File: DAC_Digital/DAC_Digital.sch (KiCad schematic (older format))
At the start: 118 parts

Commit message: Update IACSense
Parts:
- added D?: SMCJ5.0A-TR, symbol D_TVS
- added F?: FUSE_CLIP_5x20, symbol FUSE_CLIP_5x20
- added J?: Conn_01x02, symbol Conn_01x02
- U?: footprint Mobi_library:QFN36-0.5 -> Housings_DFN_QFN:QFN-36-1EP_6x6mm_Pitch0.5mm
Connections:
- net labels removed: GND
- wire segments 510 -> 521

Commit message: update footprint
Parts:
- C? (x6): footprint Mobi_library:SM0402-MR -> Yame_library:SM0603-MR
- C? (x7), R? (x5): footprint (none) -> Yame_library:SM0603-MR
- U? (x2): value 74AHC1G08 -> 74LVC1G08
- X?: footprint Mobi_library:7A_SERIES_TXC -> Yame_library:7A_SERIES_TXC
- Y?: footprint (none) -> Crystals:Crystal_HC49-U_Vertical
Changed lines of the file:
@@
 F 0 "X?" H 11150 7200 60  0000 C CNN
 F 1 "7A-24.000MAAJ-T" H 11350 6700 60  0000 C CNN
-F 2 "Mobi_library:7A_SERIES_TXC" H 11300 6950 60  0001 C CNN
+F 2 "Yame_library:7A_SERIES_TXC" H 11300 6950 60  0001 C CNN
 F 3 "~" H 11300 6950 60  0000 C CNN
 F 4 "Crystals 24.000MHz 30ppm -20 +70C 18pF" H 11300 6950 60  0001 C CNN "Supplier Ref."
@@
 F 0 "C?" H 14650 3600 40  0000 L CNN
 F 1 "100n" H 14656 3415 40  0000 L CNN
-F 2 "Mobi_library:SM0402-MR" H 14688 3350 30  0001 C CNN
+F 2 "Yame_library:SM0603-MR" H 14688 3350 30  0001 C CNN
 F 3 "~" H 14650 3500 60  0000 C CNN
 F 4 "Capacitor MLCC 100nF 0402 10V (min.) 10%" H 14650 3500 60  0001 C CNN "Supplier Ref."
@@
 F 0 "C?" H 14450 3600 40  0000 L CNN
 F 1 "100n" H 14456 3415 40  0000 L CNN
-F 2 "Mobi_library:SM0402-MR" H 14488 3350 30  0001 C CNN
+F 2 "Yame_library:SM0603-MR" H 14488 3350 30  0001 C CNN
 F 3 "~" H 14450 3500 60  0000 C CNN
 F 4 "Capacitor MLCC 100nF 0402 10V (min.) 10%" H 14450 3500 60  0001 C CNN "Supplier Ref."
@@
 F 0 "C?" H 14250 3600 40  0000 L CNN
 F 1 "100n" H 14256 3415 40  0000 L CNN
-F 2 "Mobi_library:SM0402-MR" H 14288 3350 30  0001 C CNN
+F 2 "Yame_library:SM0603-MR" H 14288 3350 30  0001 C CNN
 F 3 "~" H 14250 3500 60  0000 C CNN
 F 4 "Capacitor MLCC 100nF 0402 10V (min.) 10%" H 14250 3500 60  0001 C CNN "Supplier Ref."
@@
 F 0 "C?" H 15350 3600 40  0000 L CNN
 F 1 "100n" H 15356 3415 40  0000 L CNN
-F 2 "Mobi_library:SM0402-MR" H 15388 3350 30  0001 C CNN
+F 2 "Yame_library:SM0603-MR" H 15388 3350 30  0001 C CNN
 F 3 "~" H 15350 3500 60  0000 C CNN
 F 4 "Capacitor MLCC 100nF 0402 10V (min.) 10%" H 15350 3500 60  0001 C CNN "Supplier Ref."
@@
 F 0 "C?" H 15150 3600 40  0000 L CNN
 F 1 "100n" H 15156 3415 40  0000 L CNN
-F 2 "Mobi_library:SM0402-MR" H 15188 3350 30  0001 C CNN
+F 2 "Yame_library:SM0603-MR" H 15188 3350 30  0001 C CNN
 F 3 "~" H 15150 3500 60  0000 C CNN
 F 4 "Capacitor MLCC 100nF 0402 10V (min.) 10%" H 15150 3500 60  0001 C CNN "Supplier Ref."
@@
 F 0 "C?" H 14950 3600 40  0000 L CNN
 F 1 "100n" H 14956 3415 40  0000 L CNN
-F 2 "Mobi_library:SM0402-MR" H 14988 3350 30  0001 C CNN
+F 2 "Yame_library:SM0603-MR" H 14988 3350 30  0001 C CNN
 F 3 "~" H 14950 3500 60  0000 C CNN
 F 4 "Capacitor MLCC 100nF 0402 10V (min.) 10%" H 14950 3500 60  0001 C CNN "Supplier Ref."
@@
 $Comp
 L OPA2333xxD U?
-U 1 1 59D7AFBD
+U 2 1 59D7AFBD
 P 15800 11950
 F 0 "U?" H 15800 12150 50  0000 L CNN
@@
 F 2 "" H 15800 11950 50  0001 C CNN
 F 3 "" H 15800 11950 50  0001 C CNN
-	1    15800 11950
+	2    15800 11950
 	-1   0    0    1
 $EndComp
@@
 P 10250 11250
 F 0 "U?" H 10150 11400 50  0000 C CNN
-F 1 "74AHC1G08" H 10250 11100 50  0000 C CNN
+F 1 "74LVC1G08" H 10250 11100 50  0000 C CNN
 F 2 "" H 10250 11250 50  0001 C CNN
 F 3 "" H 10250 11250 50  0001 C CNN
@@
 P 13350 13200
 F 0 "U?" H 13250 13350 50  0000 C CNN
-F 1 "74AHC1G08" H 13350 13050 50  0000 C CNN
+F 1 "74LVC1G08" H 13350 13050 50  0000 C CNN
 F 2 "" H 13350 13200 50  0001 C CNN
 F 3 "" H 13350 13200 50  0001 C CNN
@@
 F 0 "C?" H 5275 8850 50  0000 L CNN
 F 1 "100n" H 5275 8650 50  0000 L CNN
-F 2 "" H 5288 8600 50  0001 C CNN
+F 2 "Yame_library:SM0603-MR" H 5288 8600 50  0001 C CNN
 F 3 "" H 5250 8750 50  0001 C CNN
 	1    5250 8750
@@
 F 0 "C?" H 5775 8850 50  0000 L CNN
 F 1 "100n" H 5775 8650 50  0000 L CNN
-F 2 "" H 5788 8600 50  0001 C CNN
+F 2 "Yame_library:SM0603-MR" H 5788 8600 50  0001 C CNN
 F 3 "" H 5750 8750 50  0001 C CNN
 	1    5750 8750
@@
 F 0 "C?" H 6275 8850 50  0000 L CNN
 F 1 "100n" H 6275 8650 50  0000 L CNN
-F 2 "" H 6288 8600 50  0001 C CNN
+F 2 "Yame_library:SM0603-MR" H 6288 8600 50  0001 C CNN
 F 3 "" H 6250 8750 50  0001 C CNN
 	1    6250 8750
@@
 F 0 "C?" H 6775 8850 50  0000 L CNN
 F 1 "100n" H 6775 8650 50  0000 L CNN
-F 2 "" H 6788 8600 50  0001 C CNN
+F 2 "Yame_library:SM0603-MR" H 6788 8600 50  0001 C CNN
 F 3 "" H 6750 8750 50  0001 C CNN
 	1    6750 8750
@@
 F 0 "C?" H 4775 8850 50  0000 L CNN
 F 1 "100n" H 4775 8650 50  0000 L CNN
-F 2 "" H 4788 8600 50  0001 C CNN
+F 2 "Yame_library:SM0603-MR" H 4788 8600 50  0001 C CNN
 F 3 "" H 4750 8750 50  0001 C CNN
 	1    4750 8750
@@
 F 0 "Y?" H 3900 7700 50  0000 C CNN
 F 1 "10MHz" H 3900 7400 50  0000 C CNN
-F 2 "" H 3900 7550 50  0001 C CNN
+F 2 "Crystals:Crystal_HC49-U_Vertical" H 3900 7550 50  0001 C CNN
 F 3 "" H 3900 7550 50  0001 C CNN
 	1    3900 7550
@@
 F 0 "C?" H 3625 7950 50  0000 L CNN
 F 1 "18p" H 3625 7750 50  0000 L CNN
-F 2 "" H 3638 7700 50  0001 C CNN
+F 2 "Yame_library:SM0603-MR" H 3638 7700 50  0001 C CNN
 F 3 "" H 3600 7850 50  0001 C CNN
 	1    3600 7850
@@
 F 0 "C?" H 4175 7950 50  0000 L CNN
 F 1 "18p" H 4175 7750 50  0000 L CNN
-F 2 "" H 4188 7700 50  0001 C CNN
+F 2 "Yame_library:SM0603-MR" H 4188 7700 50  0001 C CNN
 F 3 "" H 4150 7850 50  0001 C CNN
 	1    4150 7850
@@
 F 0 "R?" V 3980 7200 50  0000 C CNN
 F 1 "1M" V 3900 7200 50  0000 C CNN
-F 2 "" V 3830 7200 50  0001 C CNN
+F 2 "Yame_library:SM0603-MR" V 3830 7200 50  0001 C CNN
 F 3 "" H 3900 7200 50  0001 C CNN
 	1    3900 7200
@@
 F 0 "R?" V 8130 2800 50  0000 C CNN
 F 1 "10k" V 8050 2800 50  0000 C CNN
-F 2 "" V 7980 2800 50  0001 C CNN
+F 2 "Yame_library:SM0603-MR" V 7980 2800 50  0001 C CNN
 F 3 "" H 8050 2800 50  0001 C CNN
 	1    8050 2800
@@
 F 0 "R?" V 8980 2800 50  0000 C CNN
 F 1 "10k" V 8900 2800 50  0000 C CNN
-F 2 "" V 8830 2800 50  0001 C CNN
+F 2 "Yame_library:SM0603-MR" V 8830 2800 50  0001 C CNN
 F 3 "" H 8900 2800 50  0001 C CNN
 	1    8900 2800
@@
 F 0 "R?" V 8130 3550 50  0000 C CNN
 F 1 "10k" V 8050 3550 50  0000 C CNN
-F 2 "" V 7980 3550 50  0001 C CNN
+F 2 "Yame_library:SM0603-MR" V 7980 3550 50  0001 C CNN
 F 3 "" H 8050 3550 50  0001 C CNN
 	1    8050 3550
@@
 F 0 "R?" V 8980 3550 50  0000 C CNN
 F 1 "10k" V 8900 3550 50  0000 C CNN
-F 2 "" V 8830 3550 50  0001 C CNN
+F 2 "Yame_library:SM0603-MR" V 8830 3550 50  0001 C CNN
 F 3 "" H 8900 3550 50  0001 C CNN
 	1    8900 3550

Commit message: Update footprint
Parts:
- 1M1: renamed from 1M; footprint (none) -> Yame_library:SM0603-MR
- C1, C14, C15, C16, C2, C29, C3, C38, C39, C41, C42, C5: renamed from C?; footprint (none) -> Yame_library:SM0603-MR
- C12, C13: renamed from C?; footprint Mobi_library:SM0805-MR -> Capacitors_Tantalum_SMD:CP_Tantalum_Case-U_EIA-6032-15_Hand
- C17, C18, C19, C27, C28: renamed from C?; footprint Mobi_library:SM0402-MR -> Yame_library:SM0402-MR
- C20, C21, C22, C23, C24, C26, C33, C34, C40, C43, C44: renamed from C?; footprint (none) -> Yame_library:SM0805-MR
- C25: renamed from C?; footprint Mobi_library:SM0805-MR -> Yame_library:SM0805-MR
- C30, C31, C32, C35, C36, C37: renamed from C?; footprint Yame_library:SM0603-MR -> Yame_library:SM0402-MR
- D1: renamed from D?; footprint (none) -> Diodes_SMD:D_SMC
- D2, D3: renamed from D?; footprint (none) -> Yame_library:SM0603-LED-MR
- F1: renamed from F?; footprint (none) -> Fuse_Holders_and_Fuses:Fuseholder5x20_horiz_open_universal_Type-III
- J1: renamed from J?; value Conn_01x02 -> +5V_in; footprint (none) -> Connectors:bornier2
- J10, J12, J13, J5, J6, J7, J8, J9: renamed from J?; footprint (none) -> Pin_Headers:Pin_Header_Straight_1x04_Pitch2.54mm
- J11, J14: renamed from J?; footprint (none) -> Pin_Headers:Pin_Header_Straight_2x23_Pitch2.54mm
- J2: renamed from J?; footprint (none) -> Pin_Headers:Pin_Header_Straight_1x05_Pitch2.54mm
- J3: renamed from J?; footprint (none) -> Pin_Headers:Pin_Header_Straight_1x08_Pitch2.54mm
- J4: renamed from J?; footprint (none) -> Pin_Headers:Pin_Header_Straight_1x02_Pitch2.54mm
- L1, L2: renamed from L?; value L_Core_Ferrite -> BLM18AG102SN1D; footprint (none) -> Yame_library:SM0603-MR
- Q1: renamed from Q?; value BSN20 -> 2n7002; footprint Mobi_library:SOT23-MR -> Yame_library:SOT23-MR
- Q2: renamed from Q?; value BSN20 -> 2N7002; footprint Mobi_library:SOT23-MR -> Yame_library:SOT23-MR
- Q3, Q4: renamed from Q?; footprint Mobi_library:SON(DQG)_8 -> Housings_SOIC:SOIC-8_3.9x4.9mm_Pitch1.27mm
- Q5, Q6: renamed from Q?; footprint TO_SOT_Packages_SMD:SOT-23 -> Yame_library:SOT23-MR
- R1, R10, R11, R16, R17, R18, R19, R2, R20, R27, R28, R29, R3, R30, R31, R32, R33, R34, R35, R36, R37, R38, R5: renamed from R?; footprint (none) -> Yame_library:SM0603-MR
- R21, R22, R23, R24, R25, R26: renamed from R?; footprint Mobi_library:SM0402-MR -> Yame_library:SM0402-MR
- R6, R7, R8, R9: renamed from R?; footprint Mobi_library:SM0402-MR -> Yame_library:SM0603-MR
- T1: renamed from T?; footprint (none) -> Housings_DIP:DIP-6_W10.16mm
- U1: renamed from U?; footprint (none) -> Housings_SOIC:SOIC-28W_7.5x18.7mm_Pitch1.27mm
- U3, U5: renamed from U?; value 74LVC1G08 -> 74LVC1G08GW; footprint (none) -> TO_SOT_Packages_SMD:SOT-353_SC-70-5
- U4: renamed from U?; footprint (none) -> Housings_SSOP:SSOP-28_5.3x10.2mm_Pitch0.65mm
- U7: renamed from U?; footprint (none) -> Housings_SOIC:SOIC-8_3.9x4.9mm_Pitch1.27mm
- Y1: renamed from Y?; footprint Crystals:Crystal_HC49-U_Vertical -> Crystals:Crystal_HC49-4H_Vertical
- Y2: renamed from Y?; footprint (none) -> Crystals:Crystal_HC49-4H_Vertical
- gave numbers to parts that had none: 16

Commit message: Update IACSense footprint
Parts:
- added J15, J16: Test, Pin_Headers:Pin_Header_Straight_1x08_Pitch1.00mm, symbol Conn_01x08
- J13: value Anlg_in -> Anlg_I2C
- J4: value Conn_01x02 -> Out_SPDIF
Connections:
- wire segments 521 -> 537

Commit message: place all components on DAC_Analog
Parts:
- J15, J16: footprint Pin_Headers:Pin_Header_Straight_1x08_Pitch1.00mm -> Pin_Headers:Pin_Header_Straight_1x08_Pitch1.27mm
- R39: renamed from 1M1; value R -> 1meg
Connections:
- net labels added: Vanlg
- net labels removed: +3.3V, Vcc
- wire segments 537 -> 538

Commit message: update layout DAC_Digital
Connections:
- net labels added: VDD_5V_USB1
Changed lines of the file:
@@
 	-1   0    0    -1
 $EndComp
-Text Label 15350 4450 0    60   ~ 0
-VDD_5V
+Text Label 15050 4450 0    60   ~ 0
+VDD_5V_USB1
 $Comp
 L Conn_01x04 J7
@@
 	15150 4650 15700 4650
 Wire Wire Line
-	15700 4450 15350 4450
+	15050 4450 15700 4450
 Wire Wire Line
 	16700 5500 16700 5600

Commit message: Finish DAC_Digital layout
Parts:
- added C45, C46, C47, C48: 10u, Yame_library:SM0805-MR, symbol C-RESCUE-EPM_V5
- added J17, J? (x3): Fix, Mounting_Holes:MountingHole_3.2mm_M3, symbol Conn_01x01
- added R40: 390, Yame_library:SM0603-MR, symbol R
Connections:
- wire segments 538 -> 547
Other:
- moved on the sheet: R10

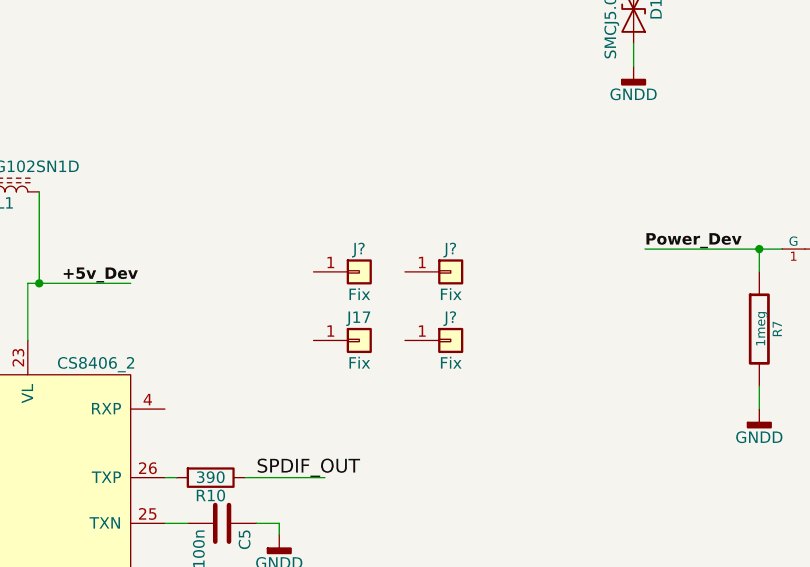
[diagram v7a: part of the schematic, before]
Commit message: Update layout DAC_Digital
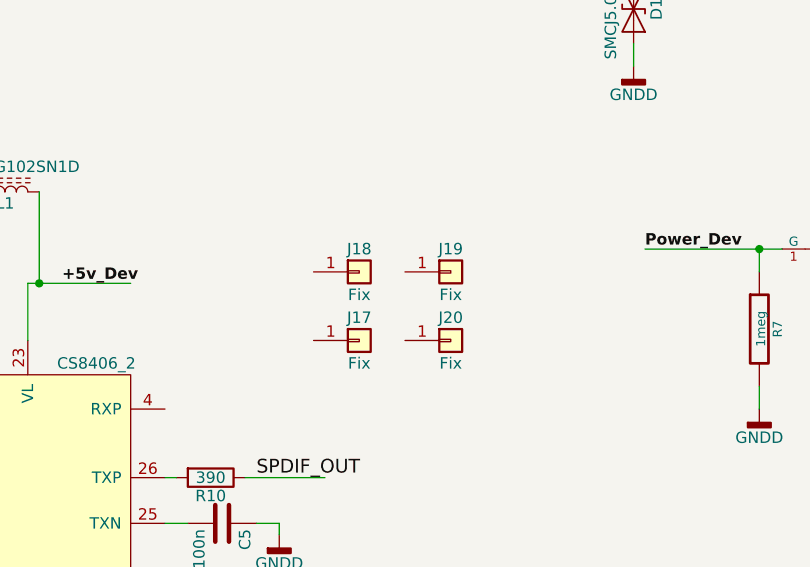
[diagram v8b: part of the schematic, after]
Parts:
- gave numbers to parts that had none: 3
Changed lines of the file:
@@
 $EndComp
 $Comp
-L Conn_01x01 J?
+L Conn_01x01 J20
 U 1 1 59EDB15F
 P 5000 12050
-F 0 "J?" H 5000 12150 50  0000 C CNN
+F 0 "J20" H 5000 12150 50  0000 C CNN
 F 1 "Fix" H 5000 11950 50  0000 C CNN
 F 2 "Mounting_Holes:MountingHole_3.2mm_M3" H 5000 12050 50  0001 C CNN
@@
 $EndComp
 $Comp
-L Conn_01x01 J?
+L Conn_01x01 J18
 U 1 1 59EDB3D1
 P 4600 11750
-F 0 "J?" H 4600 11850 50  0000 C CNN
+F 0 "J18" H 4600 11850 50  0000 C CNN
 F 1 "Fix" H 4600 11650 50  0000 C CNN
 F 2 "Mounting_Holes:MountingHole_3.2mm_M3" H 4600 11750 50  0001 C CNN
@@
 $EndComp
 $Comp
-L Conn_01x01 J?
+L Conn_01x01 J19
 U 1 1 59EDB3D7
 P 5000 11750
-F 0 "J?" H 5000 11850 50  0000 C CNN
+F 0 "J19" H 5000 11850 50  0000 C CNN
 F 1 "Fix" H 5000 11650 50  0000 C CNN
 F 2 "Mounting_Holes:MountingHole_3.2mm_M3" H 5000 11750 50  0001 C CNN
